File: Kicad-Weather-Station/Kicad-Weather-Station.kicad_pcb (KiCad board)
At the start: 2 copper layers, 48 parts, among them CON1 Solar Panel, P1 CONN_01X25, P2 CONN_01X25, P3 Rain Gauge, P4 Temperature/Humidity, P5 Wind Speed, P6 Air Pressure, P7 Battery, Q1 MMBT3904, Q2 MMBT3904, Q3 MMBT3906, Q4 SUD45P03-12-GE3, Q5 MMBT3904, Q6 MMBT3904, Q7 MMBT3904, Q8 MMBT3906, Q9 SUD45P03-12-GE3, U1 LMV324, U2 78M05, U3 TPS77033

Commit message: Initial layout of PCB
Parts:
- added REF**: MountingHole_3-5mm, WeatherStation:MountingHole_3-5mm, F.Cu at (73.0, 99.0)
- added REF**: MountingHole_3-5mm, WeatherStation:MountingHole_3-5mm, F.Cu at (154.0, 99.0)
- added REF**: MountingHole_3-5mm, WeatherStation:MountingHole_3-5mm, F.Cu at (154.0, 60.0)
- added REF**: MountingHole_3-5mm, WeatherStation:MountingHole_3-5mm, F.Cu at (66.0, 60.0)
- moved P5 102.1 mm to (63.2, 81.0), turned to 270 degrees
- moved P1 98.1 mm to (82.5, 99.1)
- moved R13 93.8 mm to (68.5, 83.4), turned to 270 degrees
- moved P3 85.2 mm to (63.0, 99.0), turned to 270 degrees
- moved R10 83.8 mm to (68.5, 91.4), turned to 270 degrees
- moved P6 81.1 mm to (157.0, 84.3), turned to 90 degrees
- moved Q9 80.4 mm to (127.4, 67.7), turned to 180 degrees
- moved P7 77.3 mm to (157.0, 70.5), turned to 90 degrees
- moved P4 75.4 mm to (63.0, 90.0), turned to 270 degrees
- moved R14 71.9 mm to (81.1, 87.6), turned to 90 degrees
- moved JP1 70.3 mm to (75.6, 88.2), turned to 270 degrees
- moved P2 57.4 mm to (143.5, 61.0), turned to 270 degrees
- moved Q5 56.5 mm to (115.0, 72.1), turned to 180 degrees
- moved R11 55.3 mm to (114.9, 67.3), turned to 270 degrees
- moved Q7 52.3 mm to (120.3, 67.5), turned to 180 degrees
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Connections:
- U2 pad 1: (no net) -> Net-(Q9-Pad2)
- U2 pad 2: (no net) -> Net-(R17-Pad1)
- U2 pad 3: (no net) -> Net-(D1-Pad2)
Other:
- board outline added: 100 x 50 mm

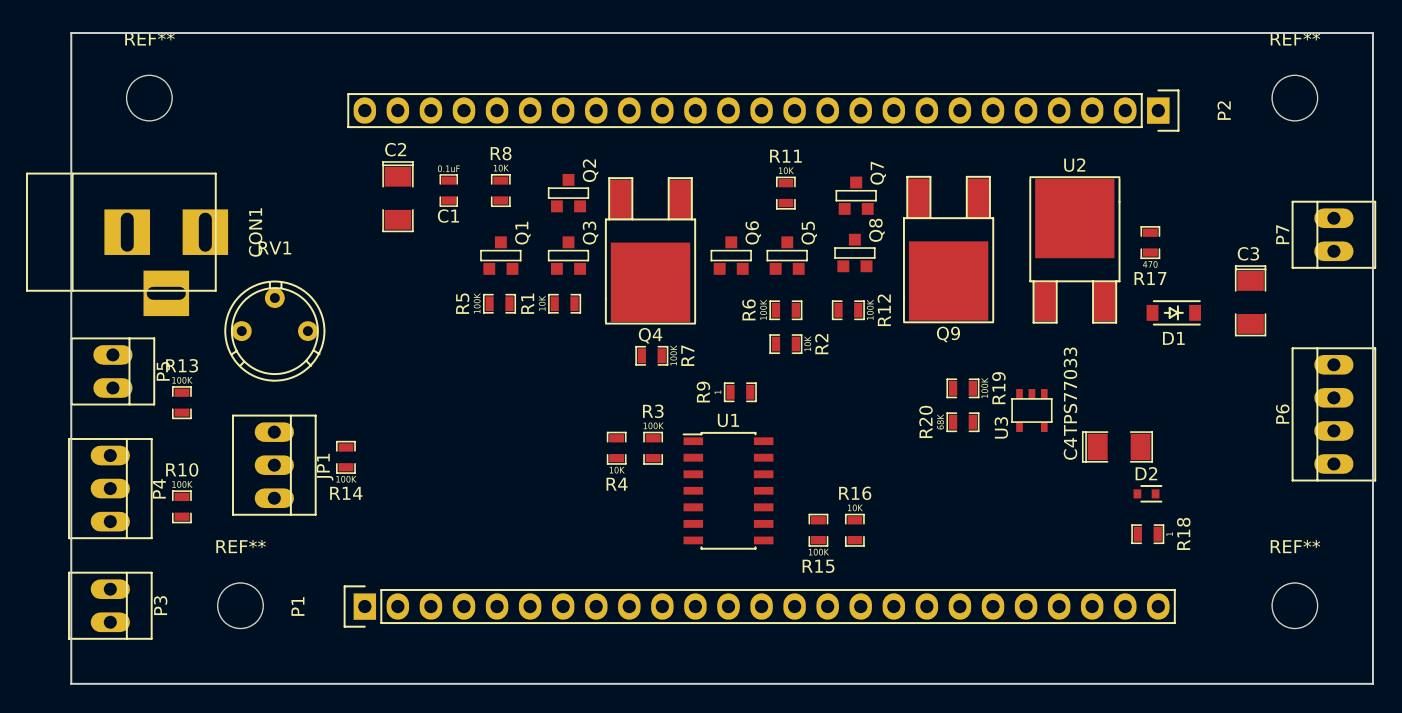
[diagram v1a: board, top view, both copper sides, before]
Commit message: Oops! forgot the microSD card. Rearrangement of PCB layout to accommodate.
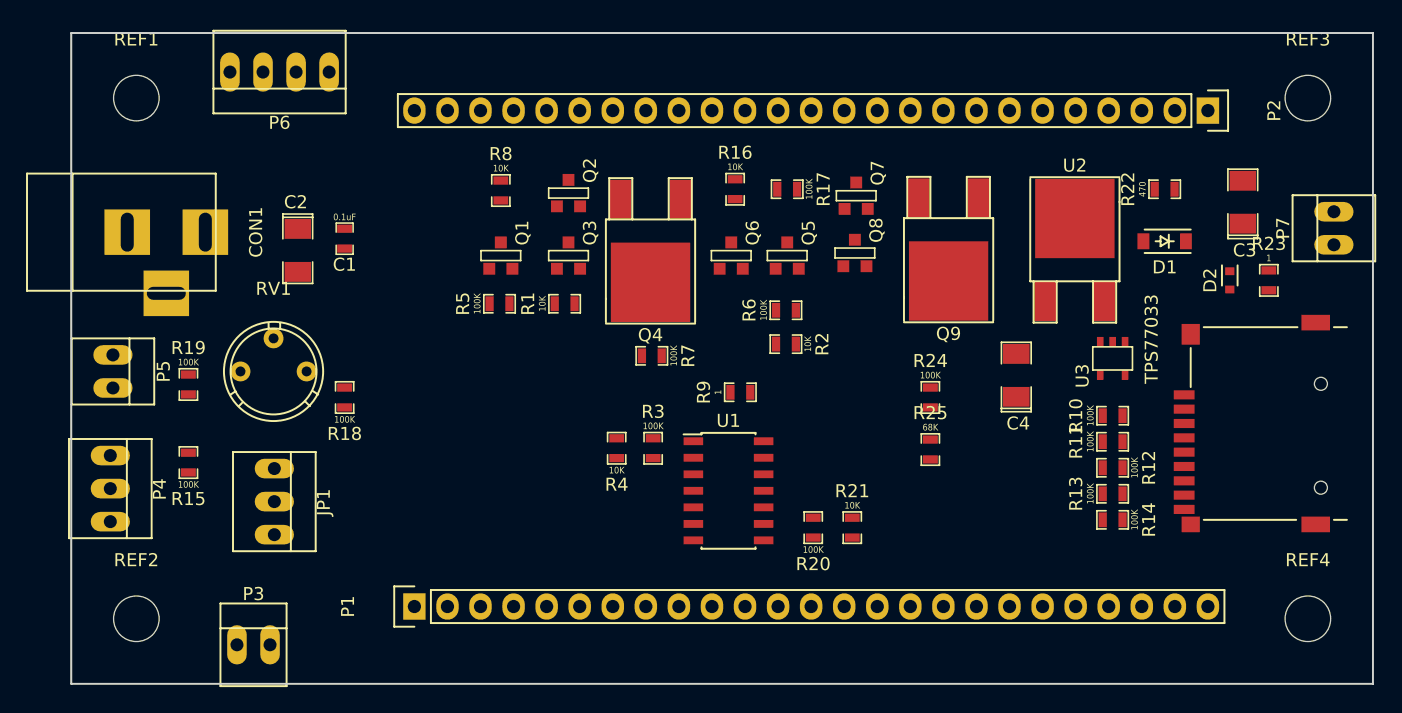
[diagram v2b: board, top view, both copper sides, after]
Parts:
- added J1: MicroSD, WeatherStation:Conn_uSDcard, F.Cu at (156.0, 85.0)
- added R21: 10K, WeatherStation:SM0603_Resistor, F.Cu at (120.0, 93.0)
- added R22: 470, WeatherStation:SM0603_Resistor, F.Cu at (144.0, 67.0)
- added R23: 1, WeatherStation:SM0603_Resistor, F.Cu at (152.0, 74.0)
- added R24: 100K, WeatherStation:SM0603_Resistor, F.Cu at (126.0, 83.0)
- added R25: 68K, WeatherStation:SM0603_Resistor, F.Cu at (126.0, 87.0)
- R11: value 10K -> 100K
- R17: value 470 -> 100K
- R18: value 1 -> 100K
- R20: value 68K -> 100K
- moved P6 85.2 mm to (76.0, 58.0), turned to 180 degrees
- moved R10 71.8 mm to (140.0, 84.4), turned to 0 degrees
- moved R13 71.8 mm to (140.0, 90.4), turned to 0 degrees
- moved R18 62.6 mm to (81.0, 83.0), turned to 90 degrees
- moved R19 59.5 mm to (69.0, 82.0), turned to 270 degrees
- moved R14 59.1 mm to (140.0, 92.4), turned to 180 degrees
- moved R15 48.7 mm to (69.0, 88.0)
- moved R11 31.5 mm to (140.0, 86.4), turned to 0 degrees
- moved R17 28.2 mm to (115.0, 67.0), turned to 180 degrees
- moved R16 27.8 mm to (111.0, 67.0)
- moved R12 23.6 mm to (140.0, 88.4)
- moved D2 17.6 mm to (149.0, 74.0), turned to 90 degrees
- moved R20 14.1 mm to (117.0, 93.0), turned to 90 degrees
- moved P3 11.4 mm to (74.0, 102.0), turned to 0 degrees
- moved C4 9.63 mm to (132.6, 81.3), turned to 90 degrees
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- renumbered REF** to REF1, REF** to REF2, REF** to REF3, REF** to REF4
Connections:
- P2 pad 6: Net-(P2-Pad6) -> PB12
- P2 pad 7: Net-(P2-Pad7) -> PB13
- P2 pad 8: Net-(P2-Pad8) -> PB14
- P2 pad 9: Net-(P2-Pad9) -> PB15
- R10 pad 2: PA0 -> PB12
- R11 pad 1: Net-(C1-Pad1) -> +3.3V
- R11 pad 2: Net-(Q5-Pad3) -> PB13
- R12 pad 1: Net-(Q7-Pad2) -> +3.3V
- R12 pad 2: Net-(Q5-Pad3) -> PB14
- R13 pad 1: PA2 -> +3.3V
- R13 pad 2: +3.3V -> PB15
- R14 pad 1: PA5 -> +3.3V
- R14 pad 2: Earth -> RSRVD
- R15 pad 1: PA7 -> +3.3V
- R15 pad 2: Net-(R15-Pad2) -> PA0
- R16 pad 1: Net-(R15-Pad2) -> Net-(C1-Pad1)
- R16 pad 2: Earth -> Net-(Q5-Pad3)
- R17 pad 1: Net-(R17-Pad1) -> Net-(Q7-Pad2)
- R17 pad 2: Earth -> Net-(Q5-Pad3)
- R18 pad 1: Net-(D2-Pad1) -> PA5
- R19 pad 1: Net-(C3-Pad1) -> PA2
- R19 pad 2: PA6 -> +3.3V
- R20 pad 1: PA6 -> PA7
- R20 pad 2: Earth -> Net-(R20-Pad2)
- U1 pad 6: Net-(R17-Pad1) -> Net-(R22-Pad1)
- U1 pad 7: Net-(R17-Pad1) -> Net-(R22-Pad1)
- U1 pad 9: Net-(R15-Pad2) -> Net-(R20-Pad2)
- U2 pad 2: Net-(R17-Pad1) -> Net-(R22-Pad1)

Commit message: First form of PCB
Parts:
- added P10: CONN_01X01, WeatherStation:SIL-1, F.Cu at (82.2, 88.1)
- added P11: CONN_01X01, WeatherStation:SIL-1, F.Cu at (123.9, 94.9)
- added P12: CONN_01X01, WeatherStation:SIL-1, F.Cu at (148.0, 89.4)
- added P8: CONN_01X01, WeatherStation:SIL-1, F.Cu at (121.9, 77.5)
- added P9: CONN_01X01, WeatherStation:SIL-1, F.Cu at (117.8, 81.9)
- C4: value 100uF -> 10uF
- moved R15 13.8 mm to (78.5, 98.0), turned to 270 degrees
- moved R18 11.3 mm to (82.0, 94.3), turned to 270 degrees
- moved R13 4.90 mm to (140.0, 85.5)
- moved R11 1.10 mm to (140.0, 87.5)
- moved R12 1.10 mm to (140.0, 89.5), turned to 0 degrees
- moved R17 1.00 mm to (115.0, 68.0)
- moved R10 0.90 mm to (140.0, 83.5)
- moved R14 0.90 mm to (140.0, 91.5), turned to 0 degrees
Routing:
- net +3.3V: track 0.00 -> 195.8 mm, vias 0 -> 2
- net PB6: track 0.00 -> 115.0 mm
- net PB7: track 0.00 -> 78.4 mm
- net Net-(C1-Pad1): track 0.00 -> 68.7 mm
- net PB4: track 0.00 -> 66.3 mm, vias 0 -> 2
- net Net-(D2-Pad1): track 0.00 -> 56.9 mm, vias 0 -> 6
- net Net-(R22-Pad1): track 0.00 -> 49.5 mm, vias 0 -> 2
- net PB14: track 0.00 -> 42.6 mm, vias 0 -> 1
- net PB13: track 0.00 -> 42.1 mm, vias 0 -> 1
- net PA2: track 0.00 -> 40.1 mm
- net Net-(C3-Pad1): track 0.00 -> 38.9 mm
- net PB15: track 0.00 -> 38.8 mm, vias 0 -> 1
- net PB12: track 0.00 -> 38.2 mm, vias 0 -> 1
- net Earth: track 0.00 -> 38.1 mm, vias 0 -> 4
- net PB5: track 0.00 -> 36.3 mm, vias 0 -> 2
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- added copper zone on B.Cu, net Earth
- added copper zone on F.Cu, net Earth

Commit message: Generate Gerbers and images
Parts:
- renumbered REF2 to ?, REF4 to ?, REF3 to ?, REF1 to ?, P8 to ?, P9 to ?, P10 to ?, P11 to ?
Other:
- board text added: "Air Pressure"
- board text added: "Battery"
- board text added: "Rain Gauge"
- board text added: "Solar panel"
- board text added: "Temp/Humidity"
- board text added: "Wind Speed"

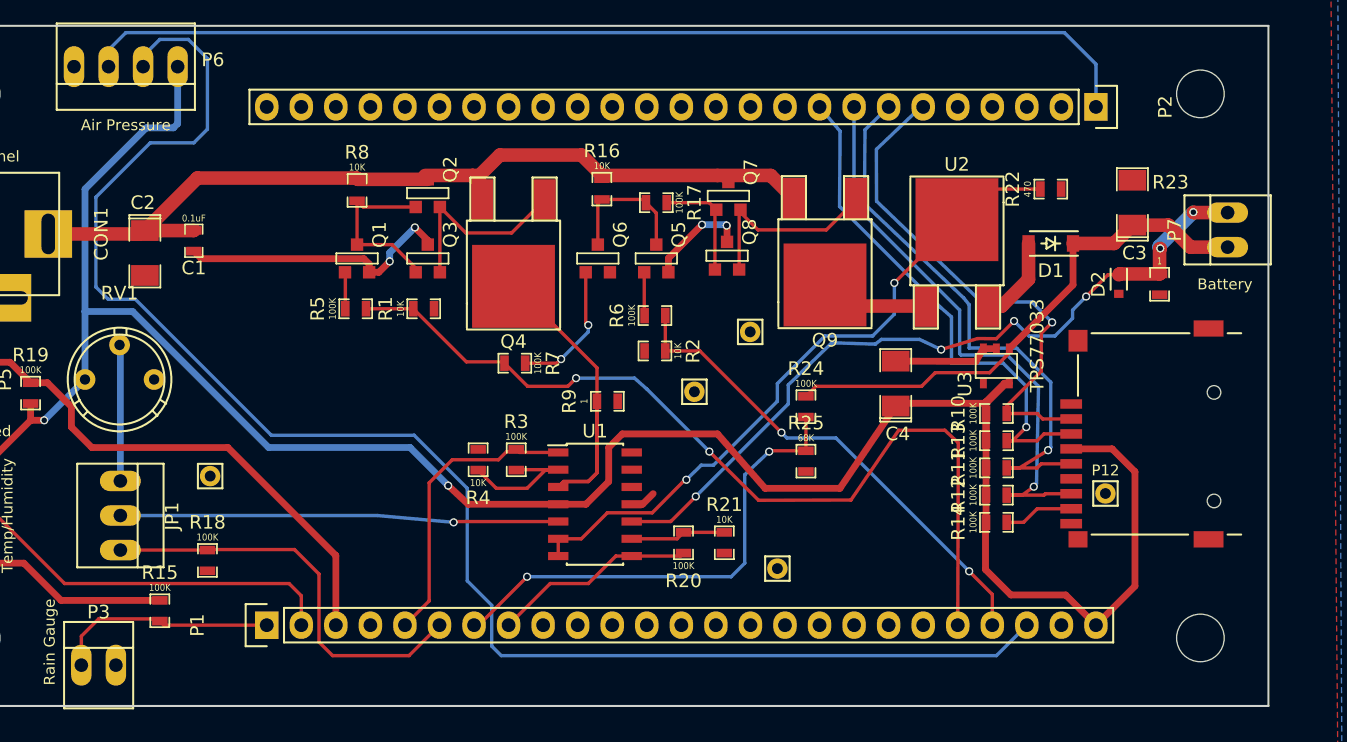
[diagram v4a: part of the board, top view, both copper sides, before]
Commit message: Add Amphenol microSD connector to PCB.
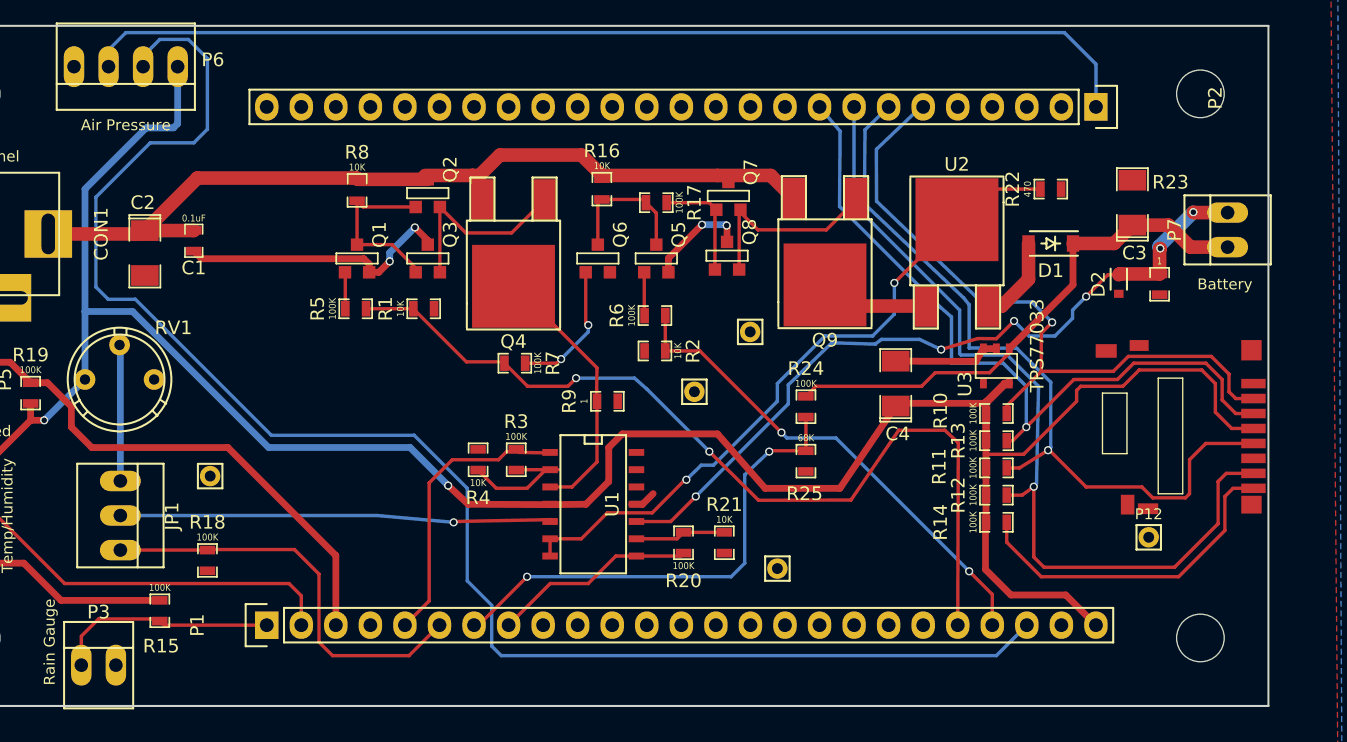
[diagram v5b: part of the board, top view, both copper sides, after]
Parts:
- J1: footprint WeatherStation:Conn_uSDcard -> WeatherStation:Conn_uSDcard_Amph_114_00841_68
- U1: footprint SOIC_Packages:SOIC-14_3.9x8.7mm_Pitch1.27mm -> WeatherStation:SOIC-14_N
- moved P12 4.53 mm to (151.2, 92.6)
- moved J1 1.87 mm to (157.8, 84.5)
- turned U1 to 270 degrees
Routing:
- net PB14: track 42.6 -> 64.1 mm
- net RSRVD: track 5.15 -> 24.8 mm
- net PB15: track 38.8 -> 54.9 mm
- net PB13: track 42.1 -> 56.9 mm
- net PB12: track 38.2 -> 51.2 mm
- net Net-(Q4-Pad2): track 28.2 -> 20.0 mm
- net +3.3V: track 195.8 -> 203.7 mm
- net Net-(R22-Pad1): track 49.5 -> 50.1 mm

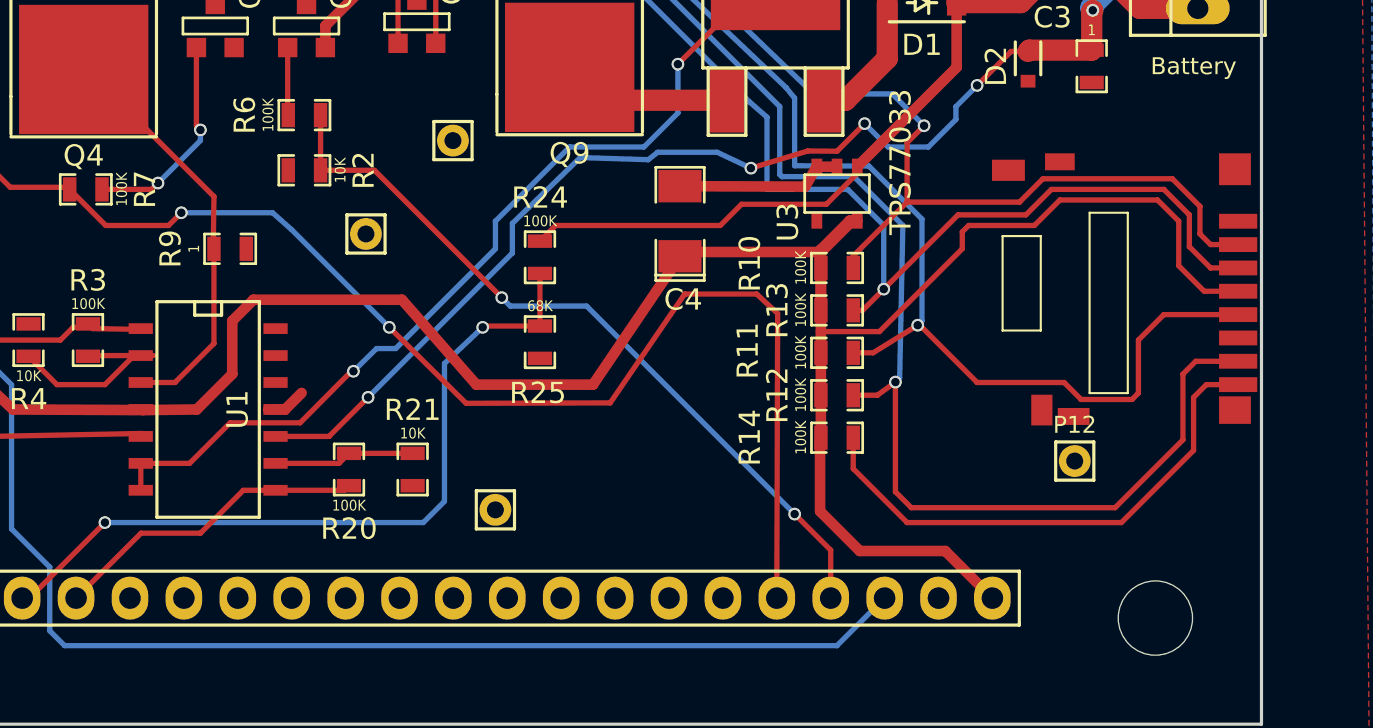
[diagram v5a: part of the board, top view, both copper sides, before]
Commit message: Add Amphenol microSD connector to PCB and add the CP (card present) signal to PA8.
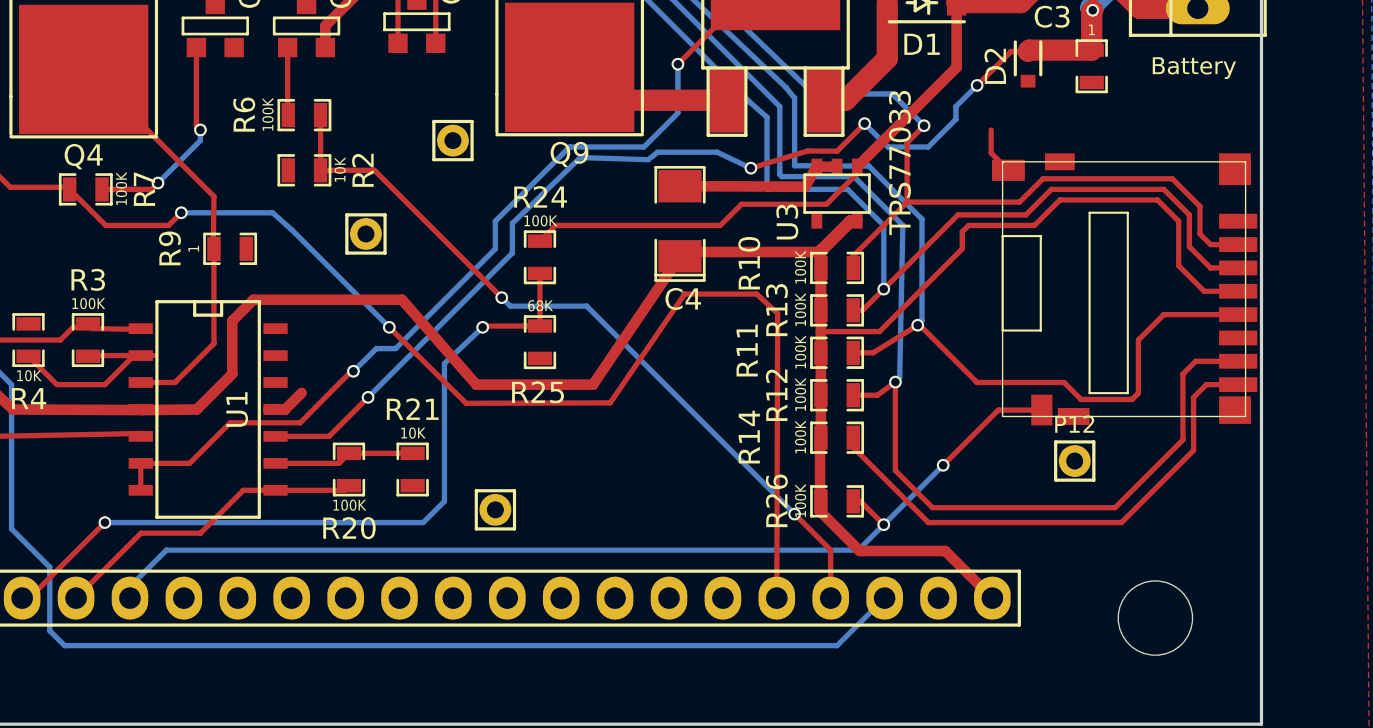
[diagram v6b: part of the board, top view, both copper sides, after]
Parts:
- added R26: 100K, WeatherStation:SM0603_Resistor, F.Cu at (140.0, 94.5)
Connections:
- J1 pad 11: (no net) -> PA8
- J1 pad 12: (no net) -> Earth
- P1 pad 9: Net-(P1-Pad9) -> PA8
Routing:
- net PA8: track 0.00 -> 48.8 mm, vias 0 -> 2
- net Earth: track 38.1 -> 40.3 mm
- net PB14: track 64.1 -> 63.5 mm
- net RSRVD: track 24.8 -> 24.2 mm
